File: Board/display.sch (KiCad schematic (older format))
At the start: 49 parts

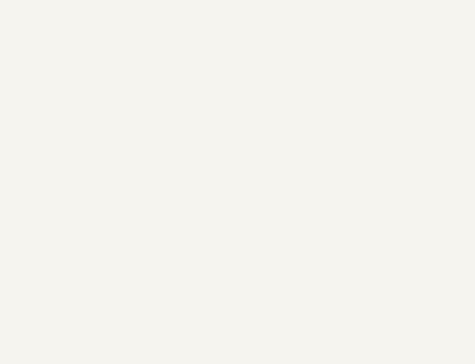
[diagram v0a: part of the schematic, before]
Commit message: [Board] Moved all other pieces into seperate hierarchical sheets.
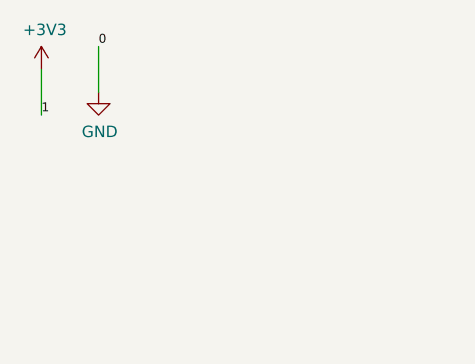
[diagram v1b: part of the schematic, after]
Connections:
- net labels added: +3V3
- wire segments 525 -> 527
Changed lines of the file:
@@
 $Descr A1 33110 23386
 encoding utf-8
-Sheet 2 2
+Sheet 2 6
 Title ""
 Date ""
@@
 Wire Wire Line
 	12500 4500 12500 5250
+$Comp
+L power:GND #PWR?
+U 1 1 616FAA0D
+P 850 850
+AR Path="/616FAA0D" Ref="#PWR?"  Part="1"
+AR Path="/64F4CB3E/616FAA0D" Ref="#PWR?"  Part="1"
+F 0 "#PWR?" H 850 600 50  0001 C CNN
+F 1 "GND" H 855 677 50  0000 C CNN
+F 2 "" H 850 850 50  0001 C CNN
+F 3 "" H 850 850 50  0001 C CNN
+	1    850  850
+	1    0    0    -1
+$EndComp
+$Comp
+L power:+3V3 #PWR?
+U 1 1 616FAA13
+P 600 750
+AR Path="/616FAA13" Ref="#PWR?"  Part="1"
+AR Path="/64F4CB3E/616FAA13" Ref="#PWR?"  Part="1"
+F 0 "#PWR?" H 600 600 50  0001 C CNN
+F 1 "+3V3" H 615 923 50  0000 C CNN
+F 2 "" H 600 750 50  0001 C CNN
+F 3 "" H 600 750 50  0001 C CNN
+	1    600  750
+	1    0    0    -1
+$EndComp
+Wire Wire Line
+	600  750  600  950
+Wire Wire Line
+	850  650  850  850
+Text Label 600  950  0    39   ~ 0
+1
+Text Label 850  650  0    39   ~ 0
+0
 $EndSCHEMATC

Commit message: [Display] Added 16x2 character display connector.
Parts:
- added DS?: HY1602E, Display:HY1602E, symbol Display_Character:HY1602E
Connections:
- no-connect marks 36 -> 39
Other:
- moved on the sheet: U?A, U?B
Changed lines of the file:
@@
 L power:GND #PWR?
 U 1 1 650EE059
-P 5800 2900
+P 5850 2750
 AR Path="/650EE059" Ref="#PWR?"  Part="1"
 AR Path="/64F4CB3E/650EE059" Ref="#PWR?"  Part="1"
-F 0 "#PWR?" H 5800 2650 50  0001 C CNN
-F 1 "GND" H 5805 2727 50  0000 C CNN
-F 2 "" H 5800 2900 50  0001 C CNN
-F 3 "" H 5800 2900 50  0001 C CNN
-	1    5800 2900
+F 0 "#PWR?" H 5850 2500 50  0001 C CNN
+F 1 "GND" H 5855 2577 50  0000 C CNN
+F 2 "" H 5850 2750 50  0001 C CNN
+F 3 "" H 5850 2750 50  0001 C CNN
+	1    5850 2750
 	-1   0    0    -1
 $EndComp
 Wire Wire Line
-	5700 2800 5800 2800
-Wire Wire Line
-	5800 2800 5800 2900
-Wire Wire Line
-	5700 2700 5800 2700
-Wire Wire Line
-	5800 2700 5800 2800
-Connection ~ 5800 2800
-Wire Wire Line
-	5800 2700 5800 2600
-Wire Wire Line
-	5800 2600 5700 2600
-Connection ~ 5800 2700
-NoConn ~ 5700 3300
-Text Label 4200 3600 0    50   ~ 0
+	5750 2650 5850 2650
+Wire Wire Line
+	5850 2650 5850 2750
+Wire Wire Line
+	5750 2550 5850 2550
+Wire Wire Line
+	5850 2550 5850 2650
+Connection ~ 5850 2650
+Wire Wire Line
+	5850 2550 5850 2450
+Wire Wire Line
+	5850 2450 5750 2450
+Connection ~ 5850 2550
+NoConn ~ 5750 3150
+Text Label 4250 3450 0    50   ~ 0
 disp_addr4
 $Comp
 L 74xx:74LS32 U?
 U 1 1 650EE069
-P 6750 3300
+P 6800 3150
 AR Path="/650EE069" Ref="U?"  Part="1"
 AR Path="/64F4CB3E/650EE069" Ref="U?"  Part="1"
-F 0 "U?" H 6650 3500 50  0000 C CNN
-F 1 "74LS32" H 6700 3100 50  0000 C CNN
-F 2 "" H 6750 3300 50  0001 C CNN
-F 3 "http://www.ti.com/lit/gpn/sn74LS32" H 6750 3300 50  0001 C CNN
-	1    6750 3300
+F 0 "U?" H 6700 3350 50  0000 C CNN
+F 1 "74LS32" H 6750 2950 50  0000 C CNN
+F 2 "" H 6800 3150 50  0001 C CNN
+F 3 "http://www.ti.com/lit/gpn/sn74LS32" H 6800 3150 50  0001 C CNN
+	1    6800 3150
 	1    0    0    1
 $EndComp
 Wire Wire Line
-	5700 3200 6450 3200
+	5750 3050 6500 3050
 $Comp
 L 74xx:74HC86 U?
 U 1 1 650EE070
-P 6050 3500
+P 6100 3350
 AR Path="/650EE070" Ref="U?"  Part="1"
 AR Path="/64F4CB3E/650EE070" Ref="U?"  Part="1"
-F 0 "U?" H 5950 3300 50  0000 C CNN
-F 1 "74HC86" H 6000 3700 50  0000 C CNN
-F 2 "" H 6050 3500 50  0001 C CNN
-F 3 "http://www.ti.com/lit/gpn/sn74HC86" H 6050 3500 50  0001 C CNN
-	1    6050 3500
-	1    0    0    -1
-$EndComp
-Wire Wire Line
-	6350 3500 6400 3500
-Wire Wire Line
-	6400 3500 6400 3400
-Wire Wire Line
-	6400 3400 6450 3400
-Wire Wire Line
-	5700 3400 5750 3400
-Wire Wire Line
-	5750 3600 4200 3600
-Wire Wire Line
-	7050 3300 7350 3300
-Text Label 7350 3300 2    50   ~ 0
+F 0 "U?" H 6000 3150 50  0000 C CNN
+F 1 "74HC86" H 6050 3550 50  0000 C CNN
+F 2 "" H 6100 3350 50  0001 C CNN
+F 3 "http://www.ti.com/lit/gpn/sn74HC86" H 6100 3350 50  0001 C CNN
+	1    6100 3350
+	1    0    0    -1
+$EndComp
+Wire Wire Line
+	6400 3350 6450 3350
+Wire Wire Line
+	6450 3350 6450 3250
+Wire Wire Line
+	6450 3250 6500 3250
+Wire Wire Line
+	5750 3250 5800 3250
+Wire Wire Line
+	5800 3450 4250 3450
+Wire Wire Line
+	7100 3150 7400 3150
+Text Label 7400 3150 2    50   ~ 0
 disp_rs
-Text Label 4450 2600 0    39   ~ 0
+Text Label 4500 2450 0    39   ~ 0
 1
-Text Label 4450 2700 0    39   ~ 0
+Text Label 4500 2550 0    39   ~ 0
 1
-Text Label 4450 2900 0    39   ~ 0
+Text Label 4500 2750 0    39   ~ 0
 0
-Text Label 4450 2800 0    39   ~ 0
+Text Label 4500 2650 0    39   ~ 0
 0
 Wire Wire Line
-	4200 3400 4700 3400
-Wire Wire Line
-	4700 3300 4200 3300
-Wire Wire Line
-	4200 3200 4700 3200
-Text Label 4200 3400 0    50   ~ 0
-disp_addr0
-Text Label 4200 3300 0    50   ~ 0
-disp_addr1
-Text Label 4200 3200 0    50   ~ 0
-disp_addr2
-Wire Wire Line
-	4200 3100 4700 3100
-Text Label 4200 3100 0    50   ~ 0
+	4250 3250 4750 3250
+Wire Wire Line
+	4750 3150 4250 3150
+Wire Wire Line
+	4250 3050 4750 3050
+Text Label 4250 3250 0    50   ~ 0
+disp_addr0
+Text Label 4250 3150 0    50   ~ 0
+disp_addr1
+Text Label 4250 3050 0    50   ~ 0
+disp_addr2
+Wire Wire Line
+	4250 2950 4750 2950
+Text Label 4250 2950 0    50   ~ 0
 disp_addr3
 Wire Wire Line
-	4450 2900 4700 2900
-Wire Wire Line
-	4450 2800 4700 2800
-Wire Wire Line
-	4450 2700 4700 2700
-Wire Wire Line
-	4450 2600 4700 2600
+	4500 2750 4750 2750
+Wire Wire Line
+	4500 2650 4750 2650
+Wire Wire Line
+	4500 2550 4750 2550
+Wire Wire Line
+	4500 2450 4750 2450
 $Comp
 L My_74xx:74HC85 U?
 U 1 1 650EE08D
-P 5200 3000
+P 5250 2850
 AR Path="/650EE08D" Ref="U?"  Part="1"
 AR Path="/64F4CB3E/650EE08D" Ref="U?"  Part="1"
-F 0 "U?" H 5200 3667 50  0000 C CNN
-F 1 "74HC85" H 5200 3576 50  0000 C CNN
-F 2 "" H 5200 3000 50  0001 C CNN
-F 3 "https://datasheet.lcsc.com/lcsc/Nexperia-74HC85D-653_C5953.pdf" H 5200 3000 50  0001 C CNN
-	1    5200 3000
+F 0 "U?" H 5250 3517 50  0000 C CNN
+F 1 "74HC85" H 5250 3426 50  0000 C CNN
+F 2 "" H 5250 2850 50  0001 C CNN
+F 3 "https://datasheet.lcsc.com/lcsc/Nexperia-74HC85D-653_C5953.pdf" H 5250 2850 50  0001 C CNN
+	1    5250 2850
 	1    0    0    -1
 $EndComp
@@
 disp_addr3
 Wire Wire Line
-	2050 3050 3150 3050
+	2100 2900 3200 2900
 $Comp
 L 74xx:74LS393 U?
 U 2 1 650EE17C
-P 2600 3300
+P 2650 3150
 AR Path="/650EE17C" Ref="U?"  Part="2"
 AR Path="/64F4CB3E/650EE17C" Ref="U?"  Part="2"
-F 0 "U?" H 2600 3050 50  0000 C CNN
-F 1 "74LS393" H 2600 2850 50  0001 C CNN
-F 2 "" H 2600 3300 50  0001 C CNN
-F 3 "74xx\\74LS393.pdf" H 2600 3300 50  0001 C CNN
-	2    2600 3300
+F 0 "U?" H 2650 2900 50  0000 C CNN
+F 1 "74LS393" H 2650 2700 50  0001 C CNN
+F 2 "" H 2650 3150 50  0001 C CNN
+F 3 "74xx\\74LS393.pdf" H 2650 3150 50  0001 C CNN
+	2    2650 3150
 	1    0    0    -1
 $EndComp
@@
 L 74xx:74LS393 U?
 U 1 1 650EE182
-P 2600 2700
+P 2650 2550
 AR Path="/650EE182" Ref="U?"  Part="1"
 AR Path="/64F4CB3E/650EE182" Ref="U?"  Part="1"
-F 0 "U?" H 2600 2450 50  0000 C CNN
-F 1 "74LS393" H 2600 2976 50  0001 C CNN
-F 2 "" H 2600 2700 50  0001 C CNN
-F 3 "74xx\\74LS393.pdf" H 2600 2700 50  0001 C CNN
-	1    2600 2700
-	1    0    0    -1
-$EndComp
-Text Label 3600 2600 2    50   ~ 0
-disp_addr0
-Text Label 3600 2700 2    50   ~ 0
-disp_addr1
-Text Label 3600 2800 2    50   ~ 0
-disp_addr2
-Text Label 3600 2900 2    50   ~ 0
+F 0 "U?" H 2650 2300 50  0000 C CNN
+F 1 "74LS393" H 2650 2826 50  0001 C CNN
+F 2 "" H 2650 2550 50  0001 C CNN
+F 3 "74xx\\74LS393.pdf" H 2650 2550 50  0001 C CNN
+	1    2650 2550
+	1    0    0    -1
+$EndComp
+Text Label 3650 2450 2    50   ~ 0
+disp_addr0
+Text Label 3650 2550 2    50   ~ 0
+disp_addr1
+Text Label 3650 2650 2    50   ~ 0
+disp_addr2
+Text Label 3650 2750 2    50   ~ 0
 disp_addr3
-Text Label 3600 3200 2    50   ~ 0
+Text Label 3650 3050 2    50   ~ 0
 disp_addr4
-NoConn ~ 3100 3300
-NoConn ~ 3100 3400
-NoConn ~ 3100 3500
-Wire Wire Line
-	3600 2600 3100 2600
-Wire Wire Line
-	3100 2700 3600 2700
-Wire Wire Line
-	3600 2800 3100 2800
-Wire Wire Line
-	3100 2900 3150 2900
-Wire Wire Line
-	3150 2900 3150 3050
-Connection ~ 3150 2900
-Wire Wire Line
-	3150 2900 3600 2900
-Wire Wire Line
-	2050 3050 2050 3200
-Wire Wire Line
-	2050 3200 2100 3200
-Text Label 1850 2900 0    50   ~ 0
+NoConn ~ 3150 3150
+NoConn ~ 3150 3250
+NoConn ~ 3150 3350
+Wire Wire Line
+	3650 2450 3150 2450
+Wire Wire Line
+	3150 2550 3650 2550
+Wire Wire Line
+	3650 2650 3150 2650
+Wire Wire Line
+	3150 2750 3200 2750
+Wire Wire Line
+	3200 2750 3200 2900
+Connection ~ 3200 2750
+Wire Wire Line
+	3200 2750 3650 2750
+Wire Wire Line
+	2100 2900 2100 3050
+Wire Wire Line
+	2100 3050 2150 3050
+Text Label 1900 2750 0    50   ~ 0
 reset
 Wire Wire Line
-	1850 2900 2100 2900
-Text Label 1850 3500 0    50   ~ 0
+	1900 2750 2150 2750
+Text Label 1900 3350 0    50   ~ 0
 reset
 Wire Wire Line
-	1850 3500 2100 3500
-Wire Wire Line
-	2100 2600 1700 2600
-Text Label 1700 2600 0    50   ~ 0
+	1900 3350 2150 3350
+Wire Wire Line
+	2150 2450 1750 2450
+Text Label 1750 2450 0    50   ~ 0
 disp_clk
 Wire Wire Line
-	3100 3200 3600 3200
+	3150 3050 3650 3050
 Wire Wire Line
 	23700 4500 23700 5250
@@
 Text Label 850  650  0    39   ~ 0
 0
+$Comp
+L Display_Character:HY1602E DS?
+U 1 1 618C0DB3
+P 28650 13100
+F 0 "DS?" H 28650 14081 50  0000 C CNN
+F 1 "HY1602E" H 28650 13990 50  0000 C CNN
+F 2 "Display:HY1602E" H 28650 12200 50  0001 C CIN
+F 3 "http://www.icbank.com/data/ICBShop/board/HY1602E.pdf" H 28850 13200 50  0001 C CNN
+	1    28650 13100
+	1    0    0    -1
+$EndComp
+Text Label 28250 13000 2    50   ~ 0
+display_bit0
+Text Label 28250 13100 2    50   ~ 0
+display_bit1
+Text Label 28250 13200 2    50   ~ 0
+display_bit2
+Text Label 28250 13300 2    50   ~ 0
+display_bit3
+Text Label 28250 13400 2    50   ~ 0
+display_bit4
+Text Label 28250 13500 2    50   ~ 0
+display_bit5
+Text Label 28250 13600 2    50   ~ 0
+display_bit6
+Text Label 28250 13700 2    50   ~ 0
+display_bit7
+Text Label 28250 12800 2    50   ~ 0
+disp_rs
+Text Label 28250 12500 2    50   ~ 0
+disp_clk
+Text Label 28250 12700 2    39   ~ 0
+0
+NoConn ~ 29050 12500
+NoConn ~ 29050 13100
+NoConn ~ 29050 13200
 $EndSCHEMATC
